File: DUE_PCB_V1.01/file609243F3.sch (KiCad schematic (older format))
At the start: 24 parts, among them J29 Motor_Right1, J30 Motor_Right2, J31 Motor_Left1, J32 Motor_Left2, J33 Cutter_Motor, J34 ODORight1, J35 ODORight2, J36 ODOLeft1, J37 ODOLeft2, J38 ODOCutter

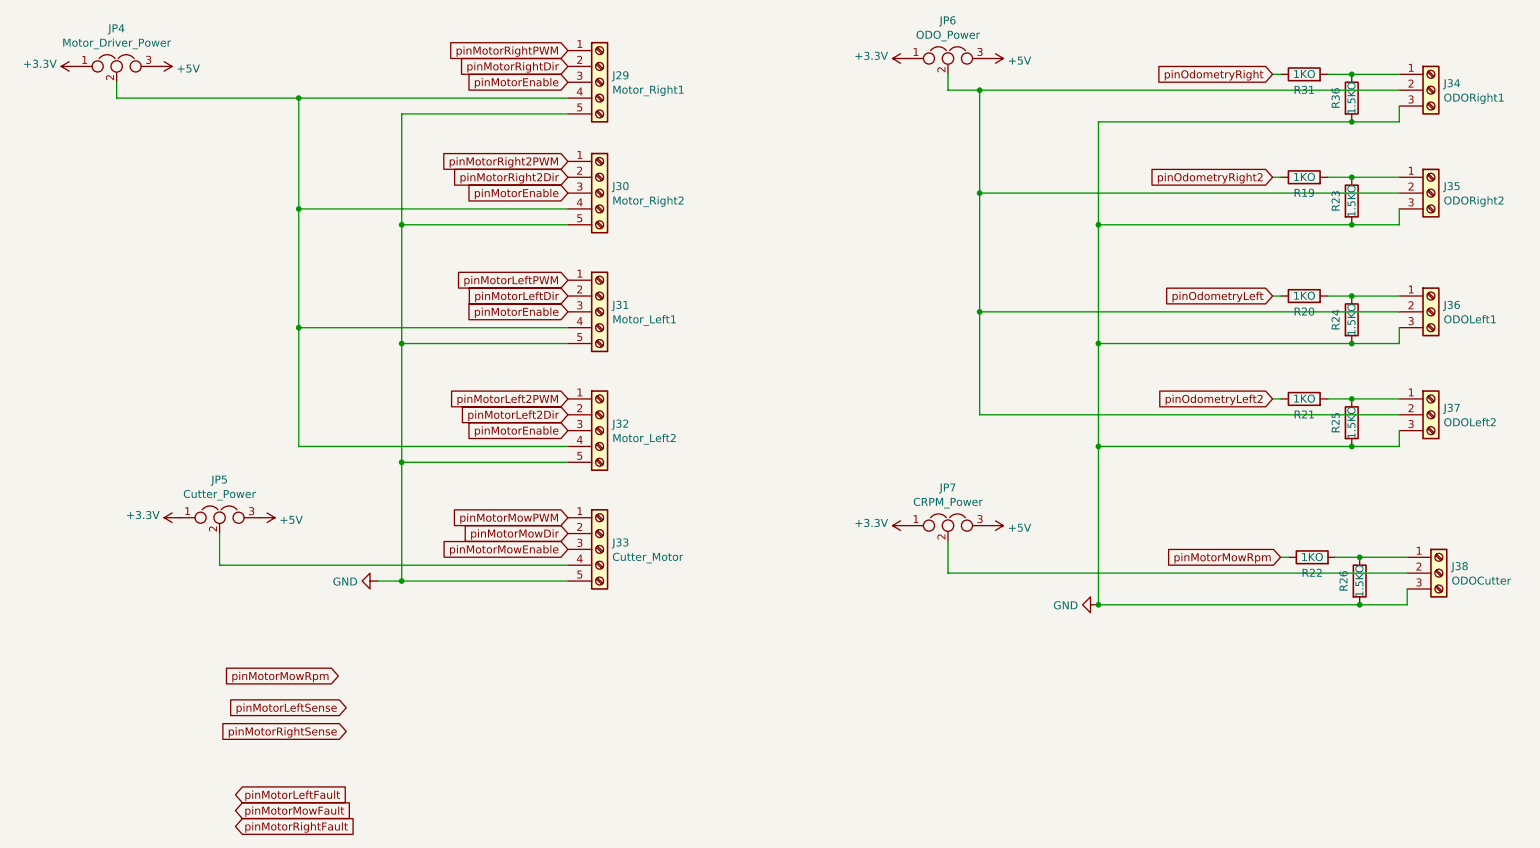
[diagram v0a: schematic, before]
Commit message: Change Pin Header to JST
Change Pin Header to JST and sort them on the PCB
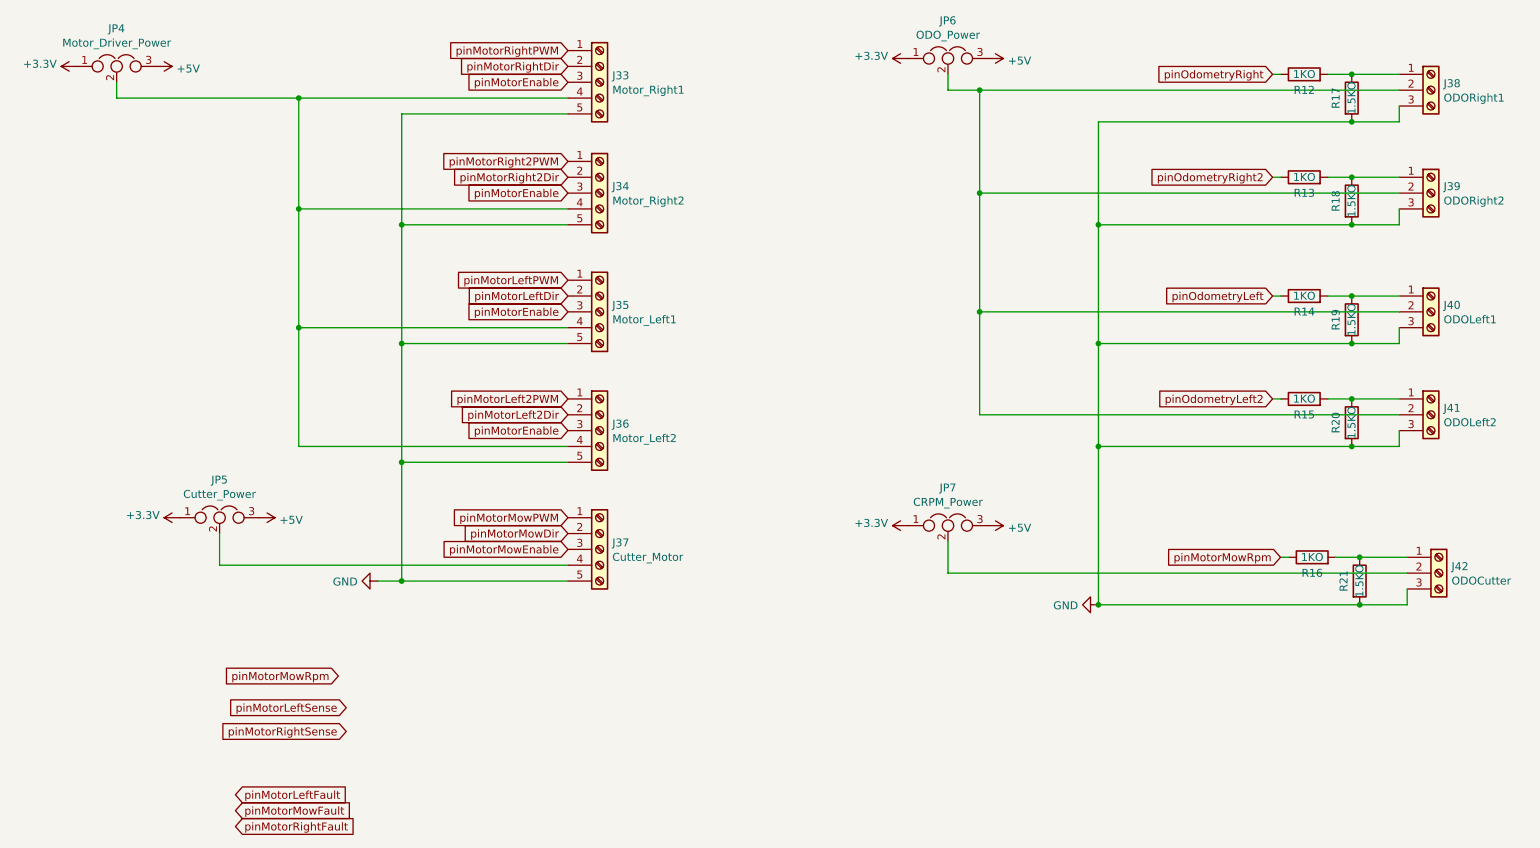
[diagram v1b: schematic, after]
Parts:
- renumbered J29 to J33, J30 to J34, J31 to J35, J32 to J36, J33 to J37, J34 to J38, J35 to J39, J36 to J40, J37 to J41, J38 to J42, R31 to R12, R19 to R13, R20 to R14, R21 to R15, R22 to R16, R36 to R17, R23 to R18, R24 to R19, R25 to R20, R26 to R21
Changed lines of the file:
@@
 P 7500 4400
 AR Path="/60C60566" Ref="#PWR?"  Part="1"
-AR Path="/609243F4/60C60566" Ref="#PWR0116"  Part="1"
-F 0 "#PWR0116" H 7500 4150 50  0001 C CNN
+AR Path="/609243F4/60C60566" Ref="#PWR076"  Part="1"
+F 0 "#PWR076" H 7500 4150 50  0001 C CNN
 F 1 "GND" V 7505 4272 50  0000 R CNN
 F 2 "" H 7500 4400 50  0001 C CNN
@@
 P 8800 1050
 AR Path="/60C6559B" Ref="R?"  Part="1"
-AR Path="/609243F4/60C6559B" Ref="R31"  Part="1"
-F 0 "R31" V 8700 1050 50  0000 C CNN
+AR Path="/609243F4/60C6559B" Ref="R12"  Part="1"
+F 0 "R12" V 8700 1050 50  0000 C CNN
 F 1 "1KO" V 8800 1050 50  0000 C CNN
 F 2 "Resistor_THT:R_Axial_DIN0207_L6.3mm_D2.5mm_P2.54mm_Vertical" V 8730 1050 50  0001 C CNN
@@
 P 9100 1200
 AR Path="/60C6D2C0" Ref="R?"  Part="1"
-AR Path="/609243F4/60C6D2C0" Ref="R36"  Part="1"
-F 0 "R36" V 9000 1200 50  0000 C CNN
+AR Path="/609243F4/60C6D2C0" Ref="R17"  Part="1"
+F 0 "R17" V 9000 1200 50  0000 C CNN
 F 1 "1.5KO" V 9100 1200 50  0000 C CNN
 F 2 "Resistor_THT:R_Axial_DIN0207_L6.3mm_D2.5mm_P2.54mm_Vertical" V 9030 1200 50  0001 C CNN
@@
 pinMotorMowRpm
 $Comp
-L Connector:Screw_Terminal_01x03 J34
+L Connector:Screw_Terminal_01x03 J38
 U 1 1 60CB0737
 P 9600 1150
-F 0 "J34" H 9680 1192 50  0000 L CNN
+F 0 "J38" H 9680 1192 50  0000 L CNN
 F 1 "ODORight1" H 9680 1101 50  0000 L CNN
 F 2 "Connector_JST:JST_XH_B3B-XH-A_1x03_P2.50mm_Vertical" H 9600 1150 50  0001 C CNN
@@
 P 8800 1700
 AR Path="/60CC3E1B" Ref="R?"  Part="1"
-AR Path="/609243F4/60CC3E1B" Ref="R19"  Part="1"
-F 0 "R19" V 8700 1700 50  0000 C CNN
+AR Path="/609243F4/60CC3E1B" Ref="R13"  Part="1"
+F 0 "R13" V 8700 1700 50  0000 C CNN
 F 1 "1KO" V 8800 1700 50  0000 C CNN
 F 2 "Resistor_THT:R_Axial_DIN0207_L6.3mm_D2.5mm_P2.54mm_Vertical" V 8730 1700 50  0001 C CNN
@@
 P 9100 1850
 AR Path="/60CC3E25" Ref="R?"  Part="1"
-AR Path="/609243F4/60CC3E25" Ref="R23"  Part="1"
-F 0 "R23" V 9000 1850 50  0000 C CNN
+AR Path="/609243F4/60CC3E25" Ref="R18"  Part="1"
+F 0 "R18" V 9000 1850 50  0000 C CNN
 F 1 "1.5KO" V 9100 1850 50  0000 C CNN
 F 2 "Resistor_THT:R_Axial_DIN0207_L6.3mm_D2.5mm_P2.54mm_Vertical" V 9030 1850 50  0001 C CNN
@@
 $EndComp
 $Comp
-L Connector:Screw_Terminal_01x03 J35
+L Connector:Screw_Terminal_01x03 J39
 U 1 1 60CC3E2F
 P 9600 1800
-F 0 "J35" H 9680 1842 50  0000 L CNN
+F 0 "J39" H 9680 1842 50  0000 L CNN
 F 1 "ODORight2" H 9680 1751 50  0000 L CNN
 F 2 "Connector_JST:JST_XH_B3B-XH-A_1x03_P2.50mm_Vertical" H 9600 1800 50  0001 C CNN
@@
 P 8800 2450
 AR Path="/60CCBFD9" Ref="R?"  Part="1"
-AR Path="/609243F4/60CCBFD9" Ref="R20"  Part="1"
-F 0 "R20" V 8700 2450 50  0000 C CNN
+AR Path="/609243F4/60CCBFD9" Ref="R14"  Part="1"
+F 0 "R14" V 8700 2450 50  0000 C CNN
 F 1 "1KO" V 8800 2450 50  0000 C CNN
 F 2 "Resistor_THT:R_Axial_DIN0207_L6.3mm_D2.5mm_P2.54mm_Vertical" V 8730 2450 50  0001 C CNN
@@
 P 9100 2600
 AR Path="/60CCBFE3" Ref="R?"  Part="1"
-AR Path="/609243F4/60CCBFE3" Ref="R24"  Part="1"
-F 0 "R24" V 9000 2600 50  0000 C CNN
+AR Path="/609243F4/60CCBFE3" Ref="R19"  Part="1"
+F 0 "R19" V 9000 2600 50  0000 C CNN
 F 1 "1.5KO" V 9100 2600 50  0000 C CNN
 F 2 "Resistor_THT:R_Axial_DIN0207_L6.3mm_D2.5mm_P2.54mm_Vertical" V 9030 2600 50  0001 C CNN
@@
 $EndComp
 $Comp
-L Connector:Screw_Terminal_01x03 J36
+L Connector:Screw_Terminal_01x03 J40
 U 1 1 60CCBFED
 P 9600 2550
-F 0 "J36" H 9680 2592 50  0000 L CNN
+F 0 "J40" H 9680 2592 50  0000 L CNN
 F 1 "ODOLeft1" H 9680 2501 50  0000 L CNN
 F 2 "Connector_JST:JST_XH_B3B-XH-A_1x03_P2.50mm_Vertical" H 9600 2550 50  0001 C CNN
@@
 P 8800 3100
 AR Path="/60CD093A" Ref="R?"  Part="1"
-AR Path="/609243F4/60CD093A" Ref="R21"  Part="1"
-F 0 "R21" V 8700 3100 50  0000 C CNN
+AR Path="/609243F4/60CD093A" Ref="R15"  Part="1"
+F 0 "R15" V 8700 3100 50  0000 C CNN
 F 1 "1KO" V 8800 3100 50  0000 C CNN
 F 2 "Resistor_THT:R_Axial_DIN0207_L6.3mm_D2.5mm_P2.54mm_Vertical" V 8730 3100 50  0001 C CNN
@@
 P 9100 3250
 AR Path="/60CD0944" Ref="R?"  Part="1"
-AR Path="/609243F4/60CD0944" Ref="R25"  Part="1"
-F 0 "R25" V 9000 3250 50  0000 C CNN
+AR Path="/609243F4/60CD0944" Ref="R20"  Part="1"
+F 0 "R20" V 9000 3250 50  0000 C CNN
 F 1 "1.5KO" V 9100 3250 50  0000 C CNN
 F 2 "Resistor_THT:R_Axial_DIN0207_L6.3mm_D2.5mm_P2.54mm_Vertical" V 9030 3250 50  0001 C CNN
@@
 $EndComp
 $Comp
-L Connector:Screw_Terminal_01x03 J37
+L Connector:Screw_Terminal_01x03 J41
 U 1 1 60CD094E
 P 9600 3200
-F 0 "J37" H 9680 3242 50  0000 L CNN
+F 0 "J41" H 9680 3242 50  0000 L CNN
 F 1 "ODOLeft2" H 9680 3151 50  0000 L CNN
 F 2 "Connector_JST:JST_XH_B3B-XH-A_1x03_P2.50mm_Vertical" H 9600 3200 50  0001 C CNN
@@
 P 8850 4100
 AR Path="/60CF2C88" Ref="R?"  Part="1"
-AR Path="/609243F4/60CF2C88" Ref="R22"  Part="1"
-F 0 "R22" V 8750 4100 50  0000 C CNN
+AR Path="/609243F4/60CF2C88" Ref="R16"  Part="1"
+F 0 "R16" V 8750 4100 50  0000 C CNN
 F 1 "1KO" V 8850 4100 50  0000 C CNN
 F 2 "Resistor_THT:R_Axial_DIN0207_L6.3mm_D2.5mm_P2.54mm_Vertical" V 8780 4100 50  0001 C CNN
@@
 P 9150 4250
 AR Path="/60CF2C92" Ref="R?"  Part="1"
-AR Path="/609243F4/60CF2C92" Ref="R26"  Part="1"
-F 0 "R26" V 9050 4250 50  0000 C CNN
+AR Path="/609243F4/60CF2C92" Ref="R21"  Part="1"
+F 0 "R21" V 9050 4250 50  0000 C CNN
 F 1 "1.5KO" V 9150 4250 50  0000 C CNN
 F 2 "Resistor_THT:R_Axial_DIN0207_L6.3mm_D2.5mm_P2.54mm_Vertical" V 9080 4250 50  0001 C CNN
@@
 $EndComp
 $Comp
-L Connector:Screw_Terminal_01x03 J38
+L Connector:Screw_Terminal_01x03 J42
 U 1 1 60CF2C9C
 P 9650 4200
-F 0 "J38" H 9730 4242 50  0000 L CNN
+F 0 "J42" H 9730 4242 50  0000 L CNN
 F 1 "ODOCutter" H 9730 4151 50  0000 L CNN
 F 2 "Connector_JST:JST_XH_B3B-XH-A_1x03_P2.50mm_Vertical" H 9650 4200 50  0001 C CNN
@@
 $EndComp
 $Comp
-L power:+3.3V #PWR069
+L power:+3.3V #PWR072
 U 1 1 60D07BCC
 P 6300 950
-F 0 "#PWR069" H 6300 800 50  0001 C CNN
+F 0 "#PWR072" H 6300 800 50  0001 C CNN
 F 1 "+3.3V" V 6315 1078 50  0000 L CNN
 F 2 "" H 6300 950 50  0001 C CNN
@@
 $EndComp
 $Comp
-L power:+5V #PWR071
+L power:+5V #PWR074
 U 1 1 60D08538
 P 6800 950
-F 0 "#PWR071" H 6800 800 50  0001 C CNN
+F 0 "#PWR074" H 6800 800 50  0001 C CNN
 F 1 "+5V" V 6815 1078 50  0000 L CNN
 F 2 "" H 6800 950 50  0001 C CNN
@@
 $EndComp
 $Comp
-L power:+3.3V #PWR070
+L power:+3.3V #PWR073
 U 1 1 60D21C76
 P 6300 3900
-F 0 "#PWR070" H 6300 3750 50  0001 C CNN
+F 0 "#PWR073" H 6300 3750 50  0001 C CNN
 F 1 "+3.3V" V 6315 4028 50  0000 L CNN
 F 2 "" H 6300 3900 50  0001 C CNN
@@
 $EndComp
 $Comp
-L power:+5V #PWR072
+L power:+5V #PWR075
 U 1 1 60D21C80
 P 6800 3900
-F 0 "#PWR072" H 6800 3750 50  0001 C CNN
+F 0 "#PWR075" H 6800 3750 50  0001 C CNN
 F 1 "+5V" V 6815 4028 50  0000 L CNN
 F 2 "" H 6800 3900 50  0001 C CNN
@@
 	6550 4200 9450 4200
 $Comp
-L Connector:Screw_Terminal_01x05 J29
+L Connector:Screw_Terminal_01x05 J33
 U 1 1 60D2D9BF
 P 4350 1100
-F 0 "J29" H 4430 1142 50  0000 L CNN
+F 0 "J33" H 4430 1142 50  0000 L CNN
 F 1 "Motor_Right1" H 4430 1051 50  0000 L CNN
 F 2 "Connector_JST:JST_XH_B5B-XH-A_1x05_P2.50mm_Vertical" H 4350 1100 50  0001 C CNN
@@
 $EndComp
 $Comp
-L Connector:Screw_Terminal_01x05 J30
+L Connector:Screw_Terminal_01x05 J34
 U 1 1 60D30152
 P 4350 1800
-F 0 "J30" H 4430 1842 50  0000 L CNN
+F 0 "J34" H 4430 1842 50  0000 L CNN
 F 1 "Motor_Right2" H 4430 1751 50  0000 L CNN
 F 2 "Connector_JST:JST_XH_B5B-XH-A_1x05_P2.50mm_Vertical" H 4350 1800 50  0001 C CNN
@@
 $EndComp
 $Comp
-L Connector:Screw_Terminal_01x05 J31
+L Connector:Screw_Terminal_01x05 J35
 U 1 1 60D32D9D
 P 4350 2550
-F 0 "J31" H 4430 2592 50  0000 L CNN
+F 0 "J35" H 4430 2592 50  0000 L CNN
 F 1 "Motor_Left1" H 4430 2501 50  0000 L CNN
 F 2 "Connector_JST:JST_XH_B5B-XH-A_1x05_P2.50mm_Vertical" H 4350 2550 50  0001 C CNN
@@
 $EndComp
 $Comp
-L Connector:Screw_Terminal_01x05 J32
+L Connector:Screw_Terminal_01x05 J36
 U 1 1 60D358E4
 P 4350 3300
-F 0 "J32" H 4430 3342 50  0000 L CNN
+F 0 "J36" H 4430 3342 50  0000 L CNN
 F 1 "Motor_Left2" H 4430 3251 50  0000 L CNN
 F 2 "Connector_JST:JST_XH_B5B-XH-A_1x05_P2.50mm_Vertical" H 4350 3300 50  0001 C CNN
@@
 $EndComp
 $Comp
-L Connector:Screw_Terminal_01x05 J33
+L Connector:Screw_Terminal_01x05 J37
 U 1 1 60D35F7E
 P 4350 4050
-F 0 "J33" H 4430 4092 50  0000 L CNN
+F 0 "J37" H 4430 4092 50  0000 L CNN
 F 1 "Cutter_Motor" H 4430 4001 50  0000 L CNN
 F 2 "Connector_JST:JST_XH_B5B-XH-A_1x05_P2.50mm_Vertical" H 4350 4050 50  0001 C CNN
@@
 P 2950 4250
 AR Path="/60D46CCC" Ref="#PWR?"  Part="1"
-AR Path="/609243F4/60D46CCC" Ref="#PWR068"  Part="1"
-F 0 "#PWR068" H 2950 4000 50  0001 C CNN
+AR Path="/609243F4/60D46CCC" Ref="#PWR071"  Part="1"
+F 0 "#PWR071" H 2950 4000 50  0001 C CNN
 F 1 "GND" V 2955 4122 50  0000 R CNN
 F 2 "" H 2950 4250 50  0001 C CNN
@@
 $EndComp
 $Comp
-L power:+3.3V #PWR066
+L power:+3.3V #PWR069
 U 1 1 60D559C9
 P 1700 3850
-F 0 "#PWR066" H 1700 3700 50  0001 C CNN
+F 0 "#PWR069" H 1700 3700 50  0001 C CNN
 F 1 "+3.3V" V 1715 3978 50  0000 L CNN
 F 2 "" H 1700 3850 50  0001 C CNN
@@
 $EndComp
 $Comp
-L power:+5V #PWR067
+L power:+5V #PWR070
 U 1 1 60D559D3
 P 2200 3850
-F 0 "#PWR067" H 2200 3700 50  0001 C CNN
+F 0 "#PWR070" H 2200 3700 50  0001 C CNN
 F 1 "+5V" V 2215 3978 50  0000 L CNN
 F 2 "" H 2200 3850 50  0001 C CNN
@@
 $EndComp
 $Comp
-L power:+3.3V #PWR064
+L power:+3.3V #PWR067
 U 1 1 60D5DD7F
 P 1050 1000
-F 0 "#PWR064" H 1050 850 50  0001 C CNN
+F 0 "#PWR067" H 1050 850 50  0001 C CNN
 F 1 "+3.3V" V 1065 1128 50  0000 L CNN
 F 2 "" H 1050 1000 50  0001 C CNN
@@
 $EndComp
 $Comp
-L power:+5V #PWR065
+L power:+5V #PWR068
 U 1 1 60D5DD89
 P 1550 1000
-F 0 "#PWR065" H 1550 850 50  0001 C CNN
+F 0 "#PWR068" H 1550 850 50  0001 C CNN
 F 1 "+5V" V 1565 1128 50  0000 L CNN
 F 2 "" H 1550 1000 50  0001 C CNN
